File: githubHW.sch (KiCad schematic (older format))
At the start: 142 parts, among them J1 Conn_01x06, J2 Conn_01x07, J3 Conn_01x07, J4 Conn_01x07, J5 Conn_01x07, J6 Conn_01x06, SW1 SW_Push, SW2 SW_Push, SW3 SW_Push, SW4 SW_Push, U1 WeMos_mini, U2 TPIC6B595N, U3 TLC5940NT, U4 TPIC6B595N

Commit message: connection issue fixed
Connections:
- net at D100.1 (K), D107.1 (K), D114.1 (K)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: now also U4.5 (DRAIN1); no longer U4.15 (DRAIN5)
- net at D106.1 (K), D113.1 (K), D120.1 (K)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: now also U4.4 (DRAIN0); no longer U4.16 (DRAIN6)
- net at D101.1 (K), D108.1 (K), D115.1 (K)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: now also U4.6 (DRAIN2); no longer U4.14 (DRAIN4)
- net at D103.1 (K), D110.1 (K), D117.1 (K)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: now also U4.14 (DRAIN4); no longer U4.6 (DRAIN2)
- net at D104.1 (K), D111.1 (K), D118.1 (K)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: now also U4.15 (DRAIN5); no longer U4.5 (DRAIN1)
- net at D105.1 (K), D112.1 (K), D119.1 (K)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: now also U4.16 (DRAIN6); no longer U4.4 (DRAIN0)
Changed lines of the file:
@@
 LIBS:contrib
 LIBS:valves
-LIBS:wemos_mini
 LIBS:tpic6b595
 LIBS:githubHW-cache
@@
 Wire Wire Line
 	2750 7800 2750 5250
-Connection ~ 9100 4000
 Wire Wire Line
 	9100 7650 9400 7650
 Wire Wire Line
-	9400 7650 9400 7900
-Connection ~ 9050 4100
-Wire Wire Line
 	9300 7700 9300 7900
 Wire Wire Line
 	9050 7700 9300 7700
-Connection ~ 9000 4200
 Wire Wire Line
 	9000 7750 9200 7750
 Wire Wire Line
 	9200 7750 9200 7900
-Connection ~ 8950 4300
 Wire Wire Line
 	9100 7800 9100 7900
 Wire Wire Line
 	8950 7800 9100 7800
-Connection ~ 8900 4400
 Wire Wire Line
 	8900 7850 9000 7850
 Wire Wire Line
 	9000 7850 9000 7900
-Connection ~ 8850 4500
 Wire Wire Line
 	8850 7900 8900 7900
-Connection ~ 8800 4600
 Wire Wire Line
 	5450 7250 9800 7250
@@
 	3950 5200 3950 5300
 Wire Wire Line
-	8800 3550 8800 7900
-Wire Wire Line
 	9150 4600 8800 4600
 Wire Wire Line
 	8850 4500 9150 4500
 Wire Wire Line
-	8850 3200 8850 7900
-Wire Wire Line
-	8900 2850 8900 7850
-Wire Wire Line
 	9150 4400 8900 4400
 Wire Wire Line
 	8950 4300 9150 4300
 Wire Wire Line
-	8950 2500 8950 7800
-Wire Wire Line
-	9000 2150 9000 7750
-Wire Wire Line
-	9150 4200 9000 4200
+	9000 2150 9000 4200
+Wire Wire Line
+	9000 4200 9150 4200
 Wire Wire Line
 	9050 4100 9150 4100
 Wire Wire Line
-	9050 1800 9050 7700
-Wire Wire Line
-	9100 1450 9100 7650
-Wire Wire Line
-	9150 4000 9100 4000
+	9050 1800 9050 4100
+Wire Wire Line
+	9100 1450 9100 4000
+Wire Wire Line
+	9100 4000 9150 4000
 Wire Wire Line
 	2000 4600 5850 4600
 Wire Wire Line
-	5850 4600 5850 3550
-Wire Wire Line
-	5800 4500 5800 3200
+	5850 3550 5850 5700
+Wire Wire Line
+	5800 3200 5800 5650
 Wire Wire Line
 	2000 4500 5800 4500
@@
 	2000 4400 5750 4400
 Wire Wire Line
-	5750 4400 5750 2850
-Wire Wire Line
-	5700 4300 5700 2500
+	5750 2850 5750 5600
 Wire Wire Line
 	2000 4300 5700 4300
@@
 	2000 4200 5650 4200
 Wire Wire Line
-	5650 4200 5650 2150
-Wire Wire Line
-	5600 4100 5600 1800
+	5650 2150 5650 5500
+Wire Wire Line
+	5600 1800 5600 5450
 Wire Wire Line
 	2000 4100 5600 4100
@@
 	2000 4000 5550 4000
 Wire Wire Line
-	5550 4000 5550 1450
+	5550 1450 5550 5400
 Wire Wire Line
 	5050 750  8950 750
@@
 Wire Wire Line
 	950  800  1300 800
+Wire Wire Line
+	8950 2500 8950 4300
+Wire Wire Line
+	8900 2850 8900 4400
+Wire Wire Line
+	8850 3200 8850 4500
+Wire Wire Line
+	8800 3550 8800 4600
+Wire Wire Line
+	9400 7650 9400 7900
+Wire Wire Line
+	5550 5400 8800 5400
+Wire Wire Line
+	8800 5400 8800 7900
+Connection ~ 5550 4000
+Wire Wire Line
+	8850 7900 8850 5450
+Wire Wire Line
+	8850 5450 5600 5450
+Connection ~ 5600 4100
+Wire Wire Line
+	5650 5500 8900 5500
+Wire Wire Line
+	8900 5500 8900 7850
+Connection ~ 5650 4200
+Wire Wire Line
+	8950 7800 8950 5550
+Wire Wire Line
+	8950 5550 5700 5550
+Wire Wire Line
+	5700 5550 5700 2500
+Connection ~ 5700 4300
+Wire Wire Line
+	5750 5600 9000 5600
+Wire Wire Line
+	9000 5600 9000 7750
+Connection ~ 5750 4400
+Wire Wire Line
+	9050 5650 9050 7700
+Wire Wire Line
+	5800 5650 9050 5650
+Connection ~ 5800 4500
+Wire Wire Line
+	5850 5700 9100 5700
+Wire Wire Line
+	9100 5700 9100 7650
+Connection ~ 5850 4600
 $EndSCHEMATC

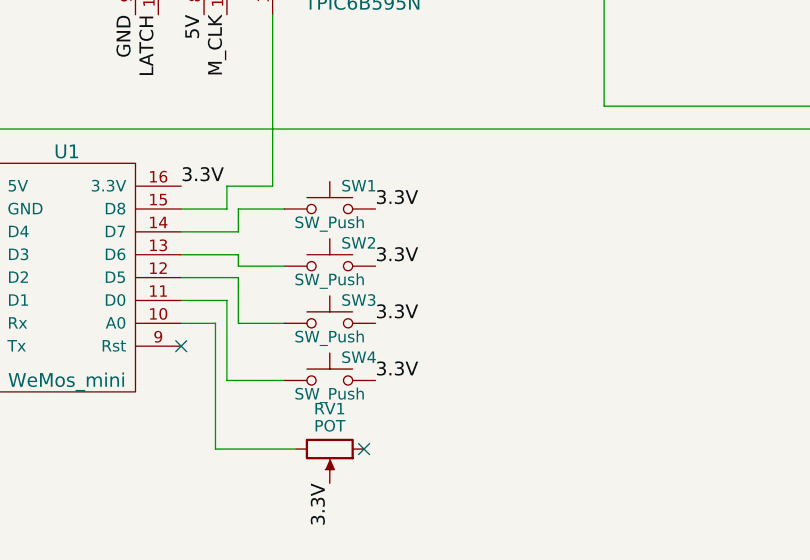
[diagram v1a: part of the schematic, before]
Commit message: buttons connection changed
now using WeMos' pullups
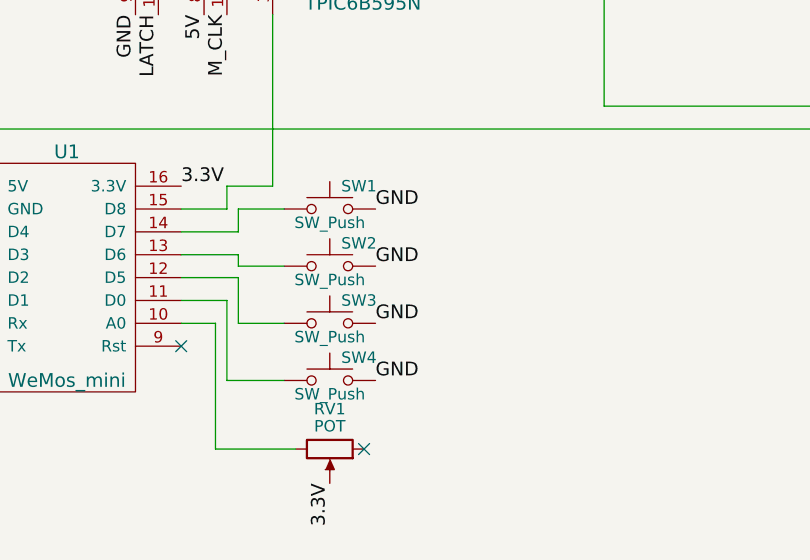
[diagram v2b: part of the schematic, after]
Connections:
- net 3.3V: no longer SW1.2, SW2.2, SW3.2, SW4.2
- net GND: now also SW1.2, SW2.2, SW3.2, SW4.2
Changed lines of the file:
@@
 Text Label 2350 9650 0    60   ~ 0
-3.3V
-Text Label 3200 9750 0    60   ~ 0
-3.3V
-Text Label 3200 10000 0    60   ~ 0
-3.3V
-Text Label 3200 10250 0    60   ~ 0
-3.3V
-Text Label 3200 10500 0    60   ~ 0
 3.3V
 Wire Wire Line
@@
 	9100 5700 9100 7650
 Connection ~ 5850 4600
+Text Label 3200 9750 0    60   ~ 0
+GND
+Text Label 3200 10000 0    60   ~ 0
+GND
+Text Label 3200 10250 0    60   ~ 0
+GND
+Text Label 3200 10500 0    60   ~ 0
+GND
 $EndSCHEMATC

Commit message: Revert "connection issue fixed"
This reverts commit d7eb6beb1c8d570a5e8c06e88c024579e6cb722b.
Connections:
- net at D100.1 (K), D107.1 (K), D114.1 (K)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: no longer U4.5 (DRAIN1)
- net at D106.1 (K), D113.1 (K), D120.1 (K)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: no longer U4.4 (DRAIN0)
- net at D101.1 (K), D108.1 (K), D115.1 (K)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: no longer U4.6 (DRAIN2)
- net at D102.1 (K), D109.1 (K), D116.1 (K)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: no longer U4.7 (DRAIN3)
- net at D103.1 (K), D110.1 (K), D117.1 (K)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: no longer U4.14 (DRAIN4)
- net at D104.1 (K), D111.1 (K), D118.1 (K)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: no longer U4.15 (DRAIN5)
- net at D105.1 (K), D112.1 (K), D119.1 (K)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: no longer U4.16 (DRAIN6)
- net at D16.1 (K), D2.1 (K), D23.1 (K)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: now also U4.15 (DRAIN5)
- net at D1.1 (K), D15.1 (K), D22.1 (K)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: now also U4.16 (DRAIN6)
- net at D10.1 (K), D17.1 (K), D24.1 (K)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: now also U4.14 (DRAIN4)
- net at D11.1 (K), D18.1 (K), D25.1 (K)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: now also U4.7 (DRAIN3)
- net at D12.1 (K), D19.1 (K), D26.1 (K)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: now also U4.6 (DRAIN2)
- net at D13.1 (K), D20.1 (K), D27.1 (K)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: now also U4.5 (DRAIN1)
- net at D14.1 (K), D21.1 (K), D28.1 (K)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: now also U4.4 (DRAIN0)
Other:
- moved on the sheet: D1, D10, D100, D101, D102, D103, D104, D105, D106, D107, D108, D109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

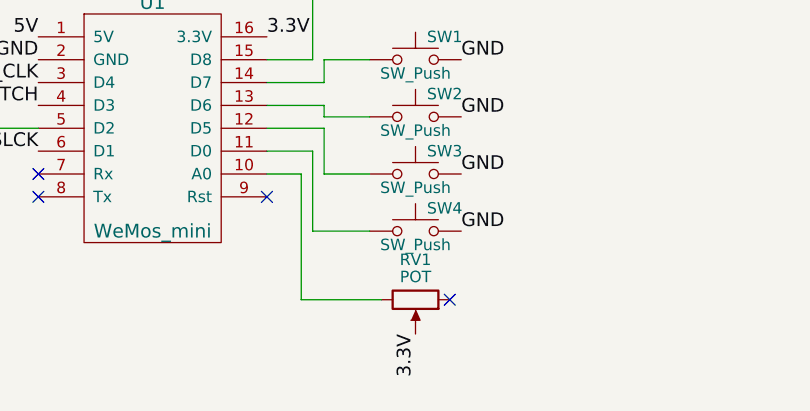
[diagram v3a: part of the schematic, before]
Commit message: poti connection corrected
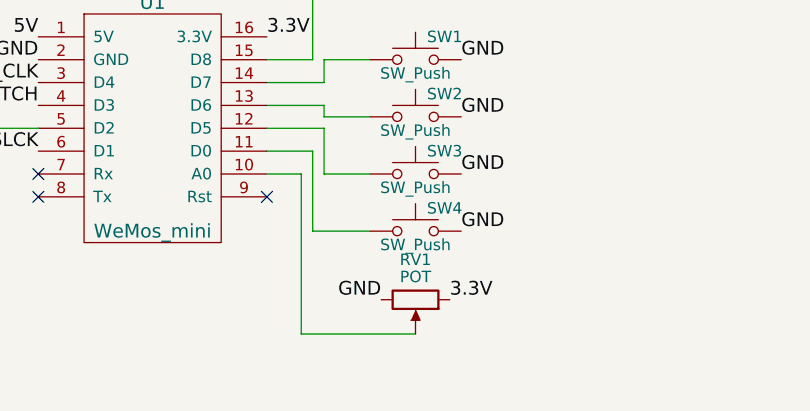
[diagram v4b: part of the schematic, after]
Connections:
- net 3.3V: now also RV1.1; no longer RV1.2
- net GND: now also RV1.3
- net at U1.10 (A0): now also RV1.2; no longer RV1.3
- no-connect marks 8 -> 7
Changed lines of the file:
@@
 	0    1    1    0
 $EndComp
-NoConn ~ 3600 10300
 $Comp
 L TPIC6B595N U2
@@
 	-1   0    0    -1
 $EndComp
-Text Label 3450 10450 3    60   ~ 0
+Text Label 3600 10300 0    60   ~ 0
 3.3V
 Text Label 2800 9150 0    60   ~ 0
@@
 	2950 9750 2800 9750
 Wire Wire Line
-	2950 10300 2950 9750
-Wire Wire Line
-	3300 10300 2950 10300
+	2950 9750 2950 10450
 Wire Wire Line
 	3000 10000 3250 10000
@@
 	6700 6100 6150 6100
 Connection ~ 6250 6150
+Text Label 3300 10300 2    60   ~ 0
+GND
+Wire Wire Line
+	2950 10450 3450 10450
 $EndSCHEMATC

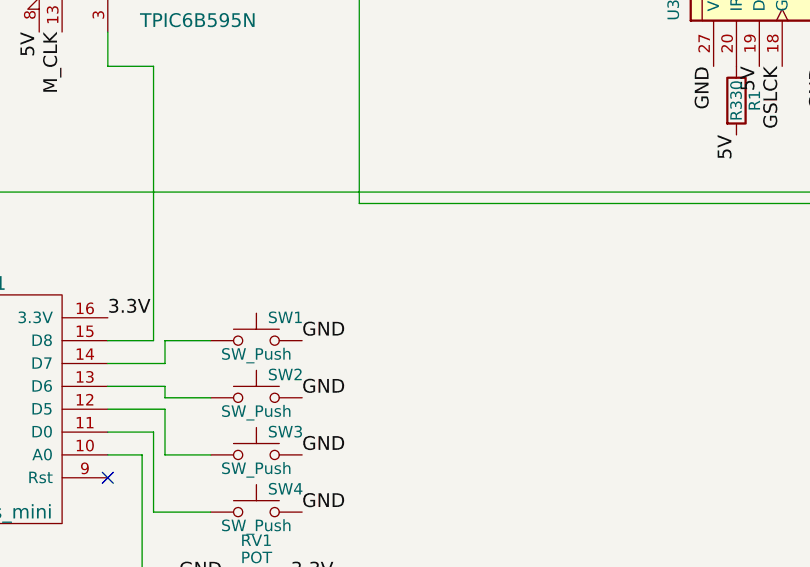
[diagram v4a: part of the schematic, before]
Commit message: wemos files commited for better usability.
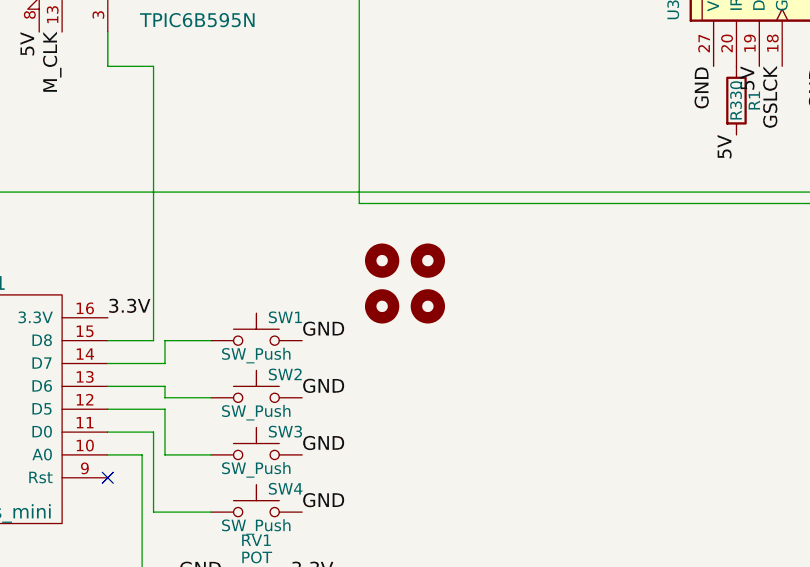
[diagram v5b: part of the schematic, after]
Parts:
- added MH1, MH2, MH3, MH4: MOUNTHOLE, Mounting_Holes:MountingHole_3.2mm_M3_ISO14580_Pad, symbol MOUNTHOLE
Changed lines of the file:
@@
 LIBS:contrib
 LIBS:valves
+LIBS:wemos_mini
 LIBS:tpic6b595
+LIBS:mounthole
 LIBS:githubHW-cache
 EELAYER 25 0
@@
 Wire Wire Line
 	2950 10450 3450 10450
+$Comp
+L MOUNTHOLE MH1
+U 1 1 5A589D03
+P 4000 8950
+F 0 "MH1" H 4150 9000 50  0001 C CNN
+F 1 "MOUNTHOLE" H 4000 9100 50  0001 C CNN
+F 2 "Mounting_Holes:MountingHole_3.2mm_M3_ISO14580_Pad" H 4000 8950 50  0001 C CNN
+F 3 "" H 4000 8950 50  0000 C CNN
+	1    4000 8950
+	1    0    0    -1
+$EndComp
+$Comp
+L MOUNTHOLE MH3
+U 1 1 5A589FDD
+P 4200 8950
+F 0 "MH3" H 4350 9000 50  0001 C CNN
+F 1 "MOUNTHOLE" H 4200 9100 50  0001 C CNN
+F 2 "Mounting_Holes:MountingHole_3.2mm_M3_ISO14580_Pad" H 4200 8950 50  0001 C CNN
+F 3 "" H 4200 8950 50  0000 C CNN
+	1    4200 8950
+	1    0    0    -1
+$EndComp
+$Comp
+L MOUNTHOLE MH2
+U 1 1 5A58A2B7
+P 4000 9150
+F 0 "MH2" H 4150 9200 50  0001 C CNN
+F 1 "MOUNTHOLE" H 4000 9300 50  0001 C CNN
+F 2 "Mounting_Holes:MountingHole_3.2mm_M3_ISO14580_Pad" H 4000 9150 50  0001 C CNN
+F 3 "" H 4000 9150 50  0000 C CNN
+	1    4000 9150
+	1    0    0    -1
+$EndComp
+$Comp
+L MOUNTHOLE MH4
+U 1 1 5A58A3E7
+P 4200 9150
+F 0 "MH4" H 4350 9200 50  0001 C CNN
+F 1 "MOUNTHOLE" H 4200 9300 50  0001 C CNN
+F 2 "Mounting_Holes:MountingHole_3.2mm_M3_ISO14580_Pad" H 4200 9150 50  0001 C CNN
+F 3 "" H 4200 9150 50  0000 C CNN
+	1    4200 9150
+	1    0    0    -1
+$EndComp
 $EndSCHEMATC

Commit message: tux added ♥
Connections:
- net at D100.1 (K), D107.1 (K), D114.1 (K)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: now also U2.15 (DRAIN5); no longer U2.5 (DRAIN1)
- net at D106.1 (K), D113.1 (K), D120.1 (K)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: now also U2.16 (DRAIN6); no longer U2.4 (DRAIN0)
- net at D101.1 (K), D108.1 (K), D115.1 (K)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: now also U2.14 (DRAIN4); no longer U2.6 (DRAIN2)
- net at D103.1 (K), D110.1 (K), D117.1 (K)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: now also U2.6 (DRAIN2); no longer U2.14 (DRAIN4)
- net at D104.1 (K), D111.1 (K), D118.1 (K)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: now also U2.5 (DRAIN1); no longer U2.15 (DRAIN5)
- net at D105.1 (K), D112.1 (K), D119.1 (K)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: now also U2.4 (DRAIN0); no longer U2.16 (DRAIN6)
